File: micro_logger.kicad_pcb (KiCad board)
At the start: 2 copper layers, 16.8 x 27.4 mm, 24 parts, among them J3 ISP, J4 Conn_01x02, J5 DM3AT-SF-PEJM5, SW2 SW_Push, U1 MIC5205-3.3, U2 MPU-9250, U3 ATMEGA328-AU, Y1 Crystal_GND2

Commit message: cleaned up layout
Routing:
- net GND: track 34.5 -> 42.3 mm
- net Net-(U3-Pad7): track 4.25 -> 2.78 mm
- net SCK: track 29.1 -> 27.8 mm
- net MOSI: track 19.3 -> 18.6 mm
- net /Ardunio/RESET: vias 3 -> 2

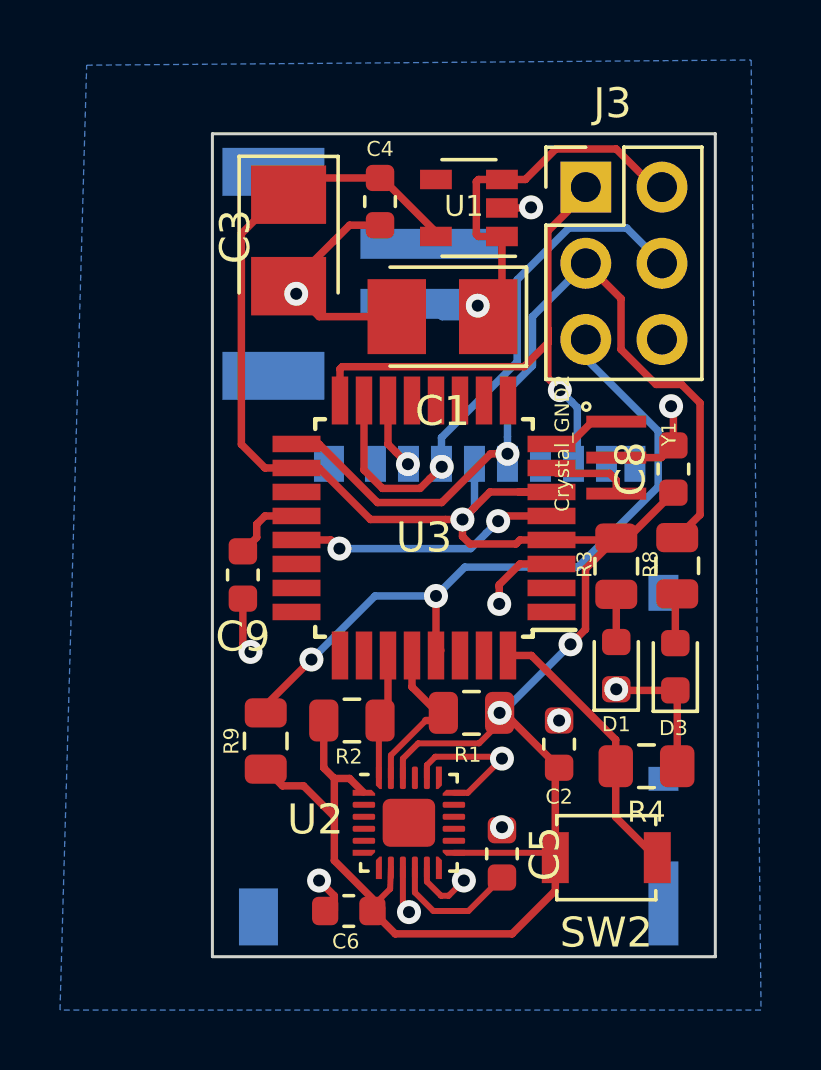
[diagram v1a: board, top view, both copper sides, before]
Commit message: added gait logo
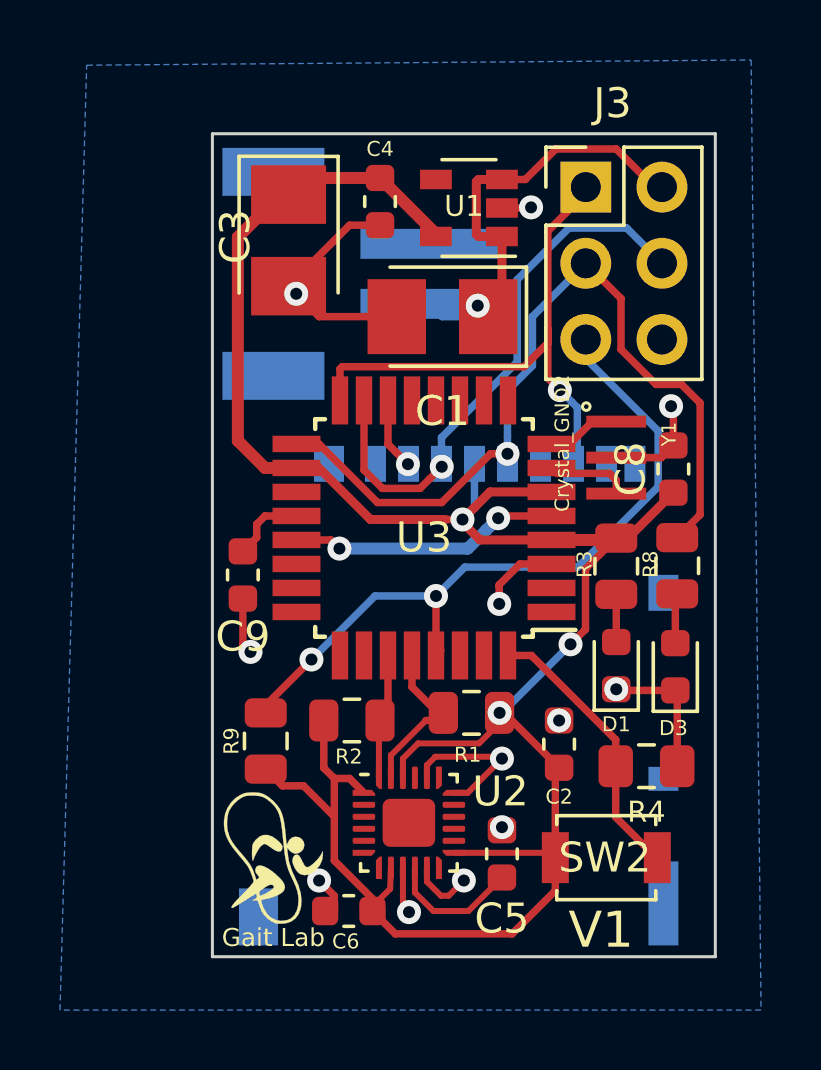
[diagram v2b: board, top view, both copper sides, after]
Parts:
- added G***: LOGO, gait_logo, F.Cu at (0.00, 0.00)
- added G***: LOGO, Symbol:gait_logo, F.Cu at (141.0, 98.6)
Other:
- board text added: "Gait Lab"
- board text added: "V1"
